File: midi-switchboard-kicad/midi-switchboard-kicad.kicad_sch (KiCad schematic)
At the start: 10 parts, among them SW1 RotaryEncoder_Switch, SW4 SW_SPDT, SW5 SW_SPDT, SW6 SW_SPDT, SW7 SW_SPDT

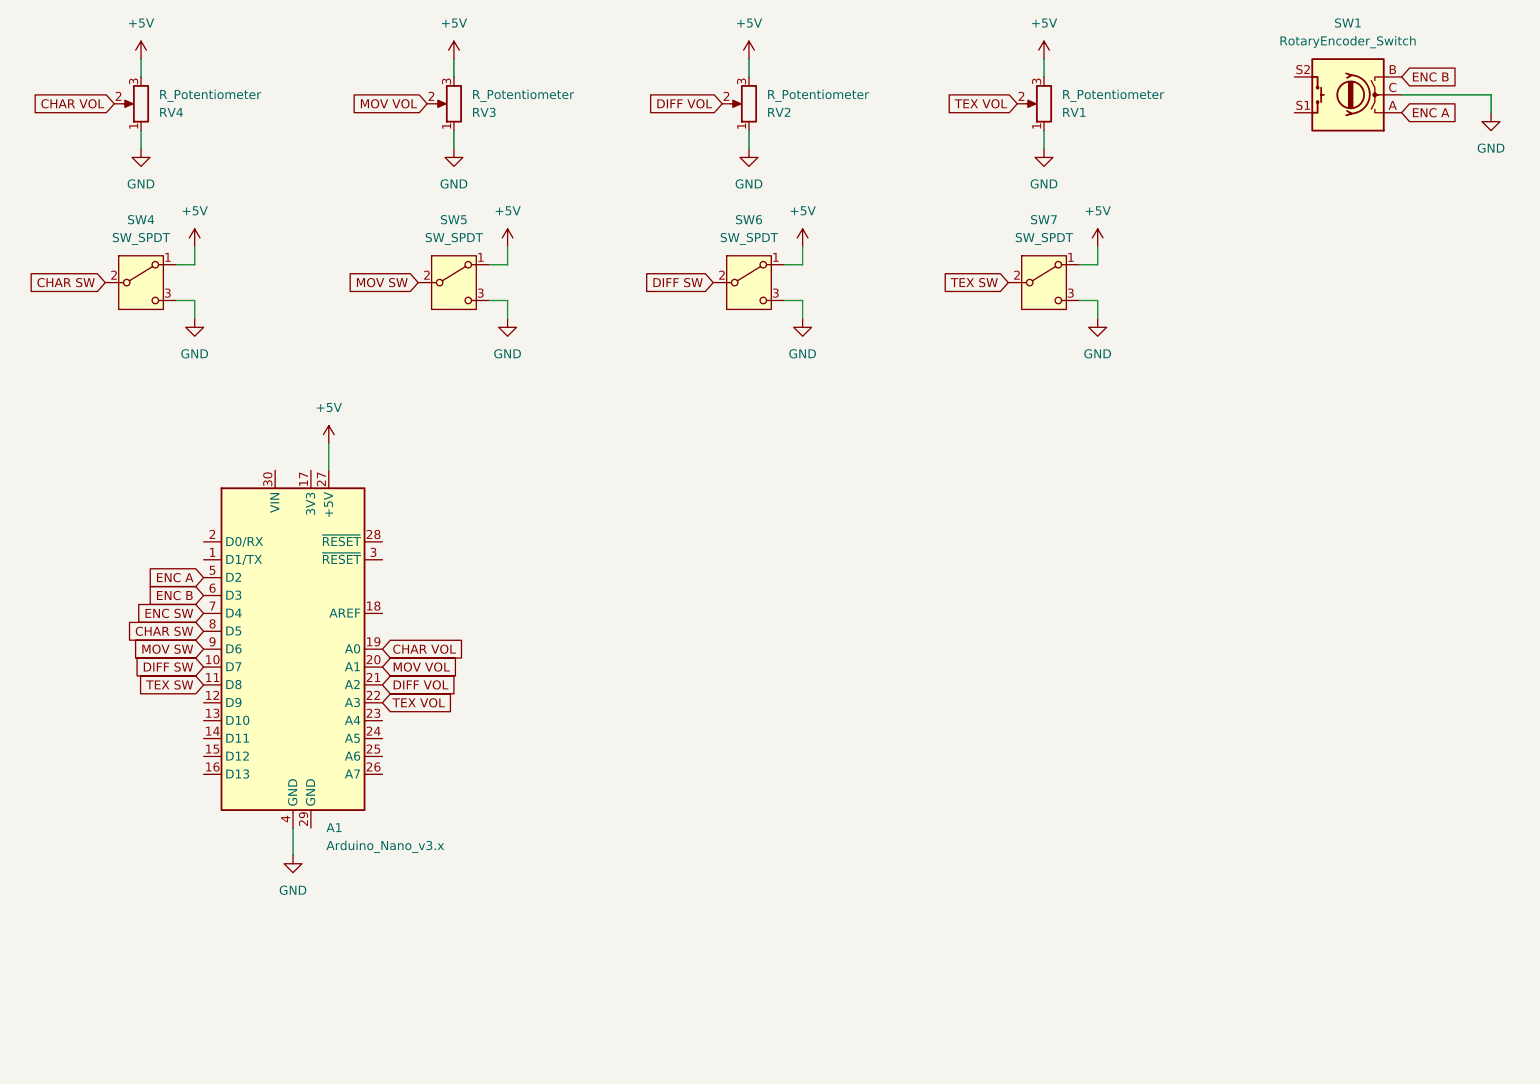
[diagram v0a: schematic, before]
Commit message: Improved potentiometer functionality
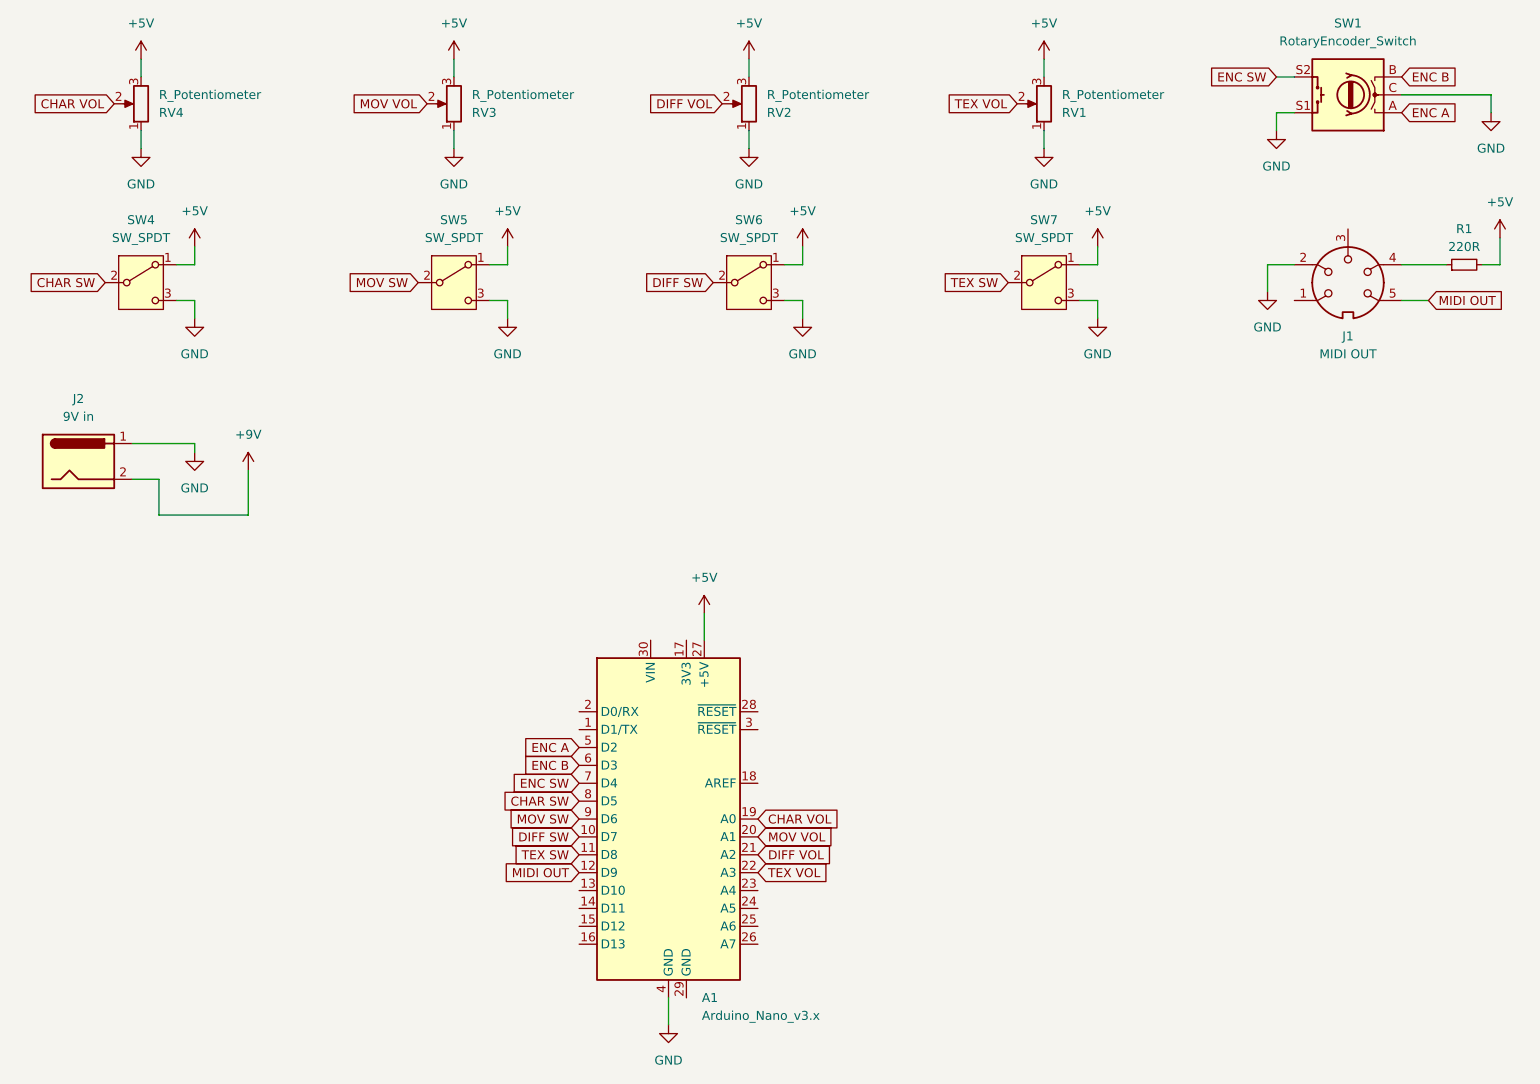
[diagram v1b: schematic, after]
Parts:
- added J1: MIDI OUT, symbol Connector:DIN-5
- added J2: 9V in, symbol Connector:Barrel_Jack
- added R1: 220R, symbol Device:R_Small
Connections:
- net +5V: now also R1.2
- net ENC SW: now also SW1.S2
- net GND: now also SW1.S1, J1.2, J2.1
- net MIDI OUT: now reaches A1.12 (D9)
- net MIDI OUT: now also J1.5
- new net: J1.4, R1.1
- new net +9V: J2.2
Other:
- moved on the sheet: A1

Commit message: Cleaned coding style and increased switch functionality
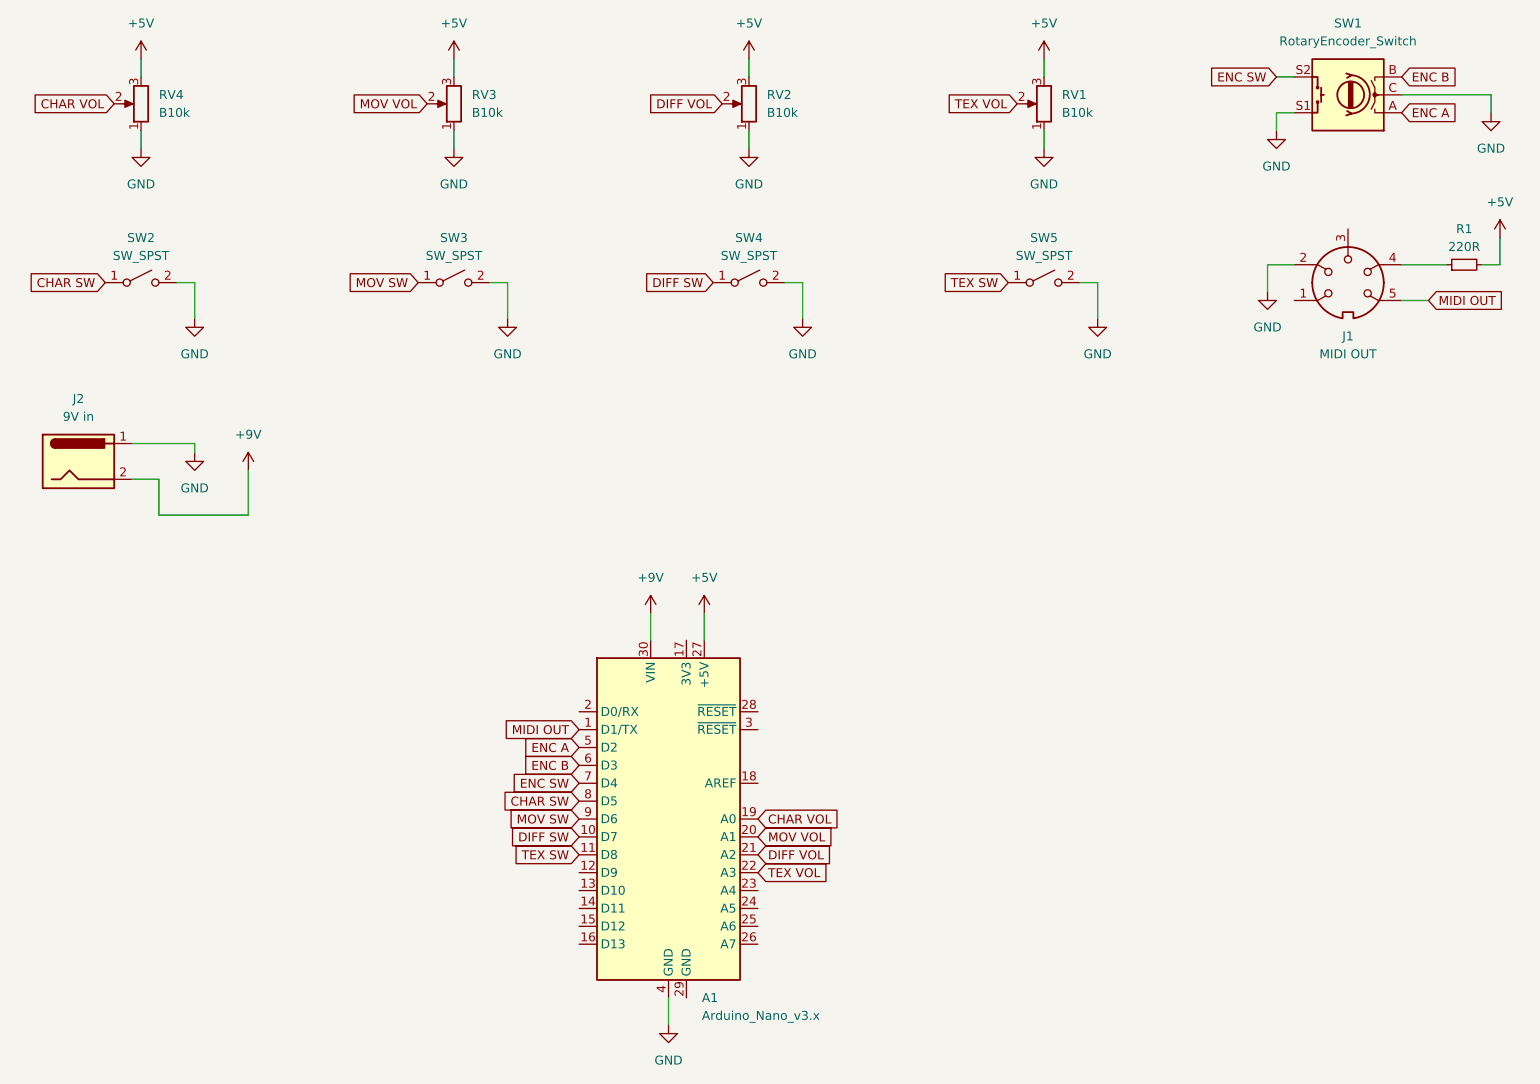
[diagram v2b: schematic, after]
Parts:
- removed SW4, SW5, SW6, SW7: SW_SPDT, symbol Switch:SW_SPDT
- added SW2, SW3, SW4, SW5: SW_SPST, symbol Switch:SW_SPST
- RV1, RV2, RV3, RV4: value R_Potentiometer -> B10k
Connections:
- net +9V: now also A1.30 (VIN)
- net CHAR SW: now also SW2.1 (A)
- net DIFF SW: now also SW4.1 (A)
- net GND: now also SW2.2 (B), SW3.2 (B), SW4.2 (B), SW5.2 (B)
- net MIDI OUT: now also A1.1 (D1/TX); no longer A1.12 (D9)
- net MOV SW: now also SW3.1 (A)
- net TEX SW: now also SW5.1 (A)
